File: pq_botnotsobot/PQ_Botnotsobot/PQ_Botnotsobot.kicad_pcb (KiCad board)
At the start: 2 copper layers, 64 x 58 mm, 16 parts, among them J1 D2FLA, J2 D2FLA1

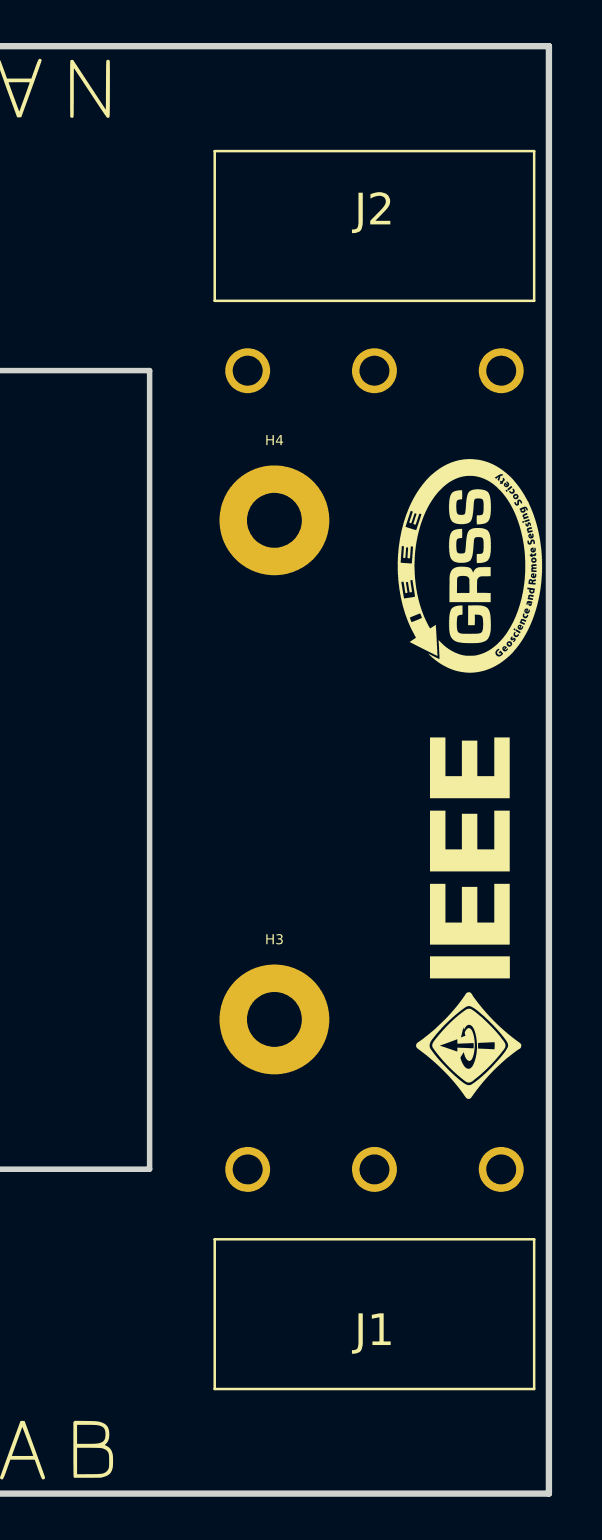
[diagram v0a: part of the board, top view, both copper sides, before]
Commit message: adjust killswitches holes to better align bottom with slider deployer PCB
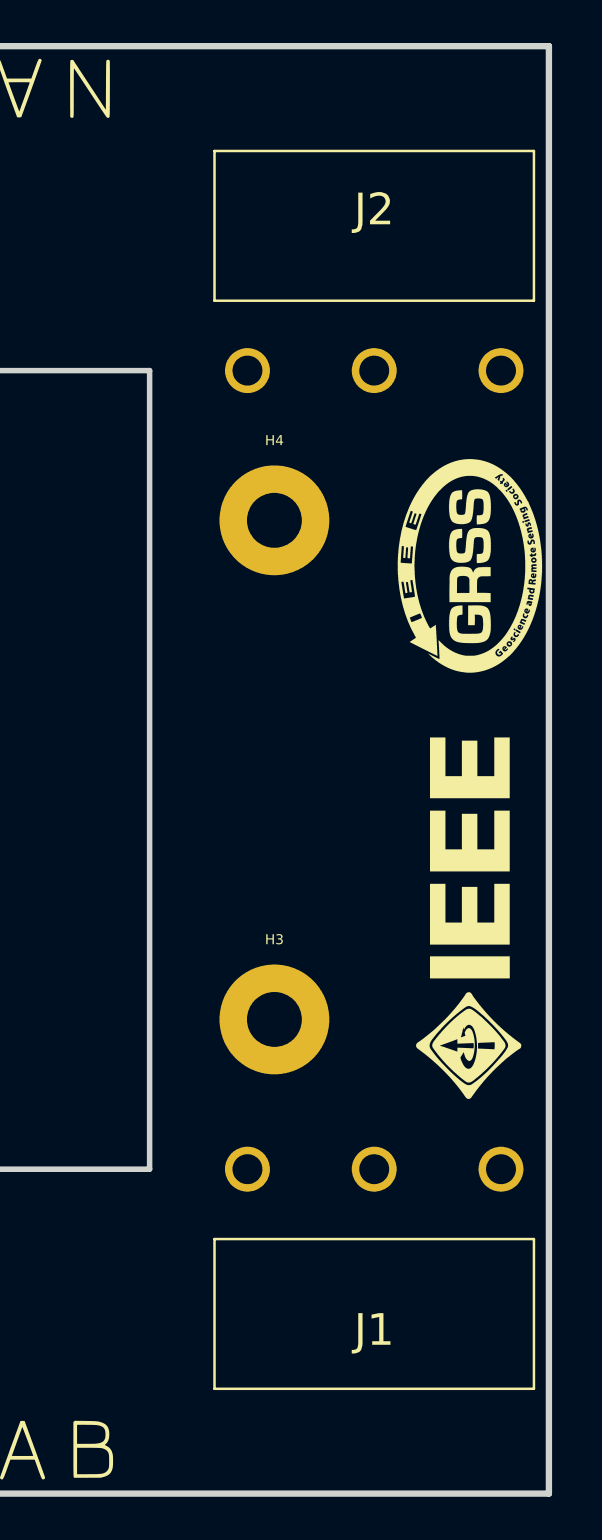
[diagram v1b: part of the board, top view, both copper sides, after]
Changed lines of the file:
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@@
   )
   (footprint "-nsl_miscellaneous:D2FLA1" (layer "F.Cu")
-    (at 132.6388 46.2788 180)
+    (at 132.63 46.274 180)
     (descr "D2F-L-A1-2")
     (tags "Switch")
@@
   )
   (footprint "-nsl_miscellaneous:D2FLA" (layer "F.Cu")
-    (at 132.6388 78.2828 180)
+    (at 132.63 78.274 180)
     (descr "D2F-L-A-3")
     (tags "Switch")

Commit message: Botboards and Latbaords corrected and revised. Production ready
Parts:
- removed H3, H4: MountingHole_Pad, MountingHole:MountingHole_2.2mm_M2_Pad
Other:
- outline, holes or cut-outs redrawn
